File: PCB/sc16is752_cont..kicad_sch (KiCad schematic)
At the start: 66 parts, among them IC13 SN74LVC1G125DBVT, IC14 LM3940IMP-3.3_NOPB, IC15 SN74LVC1G125DBVT, IC8 LMR33640ADDAR, J3 5747842-2, J4 Screw_Terminal_01x02, J5 Screw_Terminal_01x02, J6 5747842-2, Q1 SQ2319ADS-T1_BE3, Y2 ASE-14.7456MHZ-LC-T

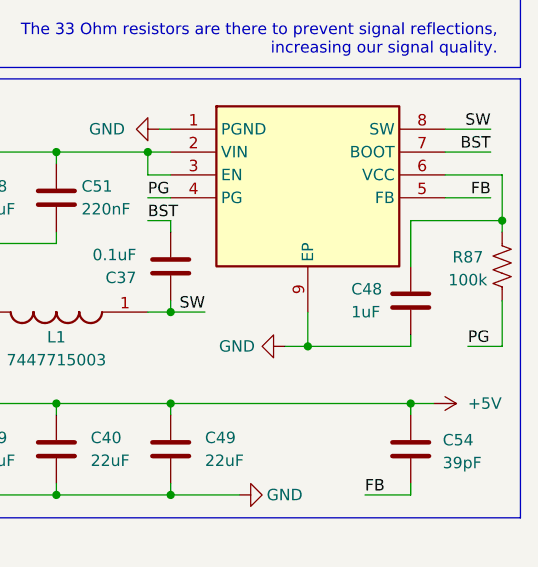
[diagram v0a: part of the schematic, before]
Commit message: Board Modifications and Initial Comms w/ Sensors
Modified wiring to separate ethernet reset from SC16 reset, adjusted pinouts and power, worked on code to get board talking to sensors. Ethernet still needs a bodge wire at this point.
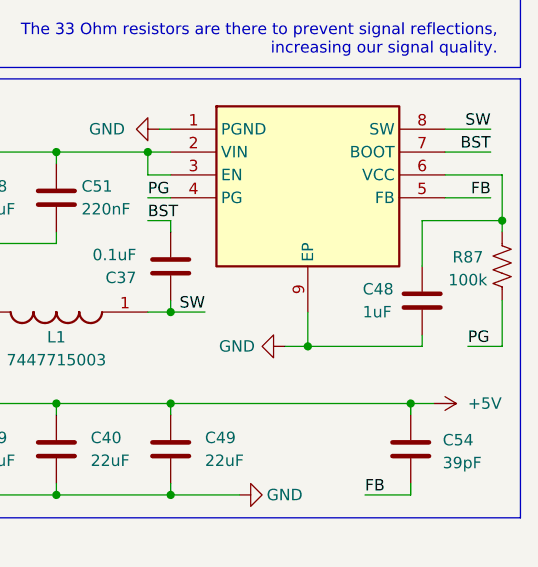
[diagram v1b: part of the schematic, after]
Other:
- moved on the sheet: C48
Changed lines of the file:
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@@
 	(wire
 		(pts
-			(xy 271.78 132.08) (xy 271.78 137.16)
+			(xy 273.05 132.08) (xy 273.05 137.16)
 		)
 		(stroke
@@
 	(wire
 		(pts
-			(xy 271.78 144.78) (xy 271.78 146.05)
+			(xy 273.05 144.78) (xy 273.05 146.05)
 		)
 		(stroke
@@
 	(wire
 		(pts
-			(xy 271.78 132.08) (xy 281.94 132.08)
+			(xy 273.05 132.08) (xy 281.94 132.08)
 		)
 		(stroke
@@
 	(wire
 		(pts
-			(xy 260.35 146.05) (xy 271.78 146.05)
+			(xy 260.35 146.05) (xy 273.05 146.05)
 		)
 		(stroke
@@
 	(symbol
 		(lib_id "Device:C")
-		(at 271.78 140.97 180)
+		(at 273.05 140.97 180)
 		(unit 1)
 		(body_style 1)
@@
 		(dnp no)
 		(property "Reference" "C48"
-			(at 265.176 139.7 0)
+			(at 266.446 139.7 0)
 			(show_name no)
 			(do_not_autoplace no)
@@
 		)
 		(property "Value" "1uF"
-			(at 265.176 142.24 0)
+			(at 266.446 142.24 0)
 			(show_name no)
 			(do_not_autoplace no)
@@
 		)
 		(property "Footprint" "Capacitor_SMD:C_0805_2012Metric_Pad1.18x1.45mm_HandSolder"
-			(at 270.8148 137.16 0)
+			(at 272.0848 137.16 0)
 			(hide yes)
 			(show_name no)
@@
 		)
 		(property "Datasheet" ""
-			(at 271.78 140.97 0)
+			(at 273.05 140.97 0)
 			(hide yes)
 			(show_name no)
@@
 		)
 		(property "Description" "Unpolarized capacitor"
-			(at 271.78 140.97 0)
+			(at 273.05 140.97 0)
 			(hide yes)
 			(show_name no)
@@
 		)
 		(property "Manufacturer_Part_Number" "CL21B105KOFNNWE"
-			(at 271.78 140.97 0)
+			(at 273.05 140.97 0)
 			(hide yes)
 			(show_name no)
@@
 		)
 		(property "Mouser Part Number" "187-CL21B105KOFNNWE"
-			(at 271.78 140.97 0)
+			(at 273.05 140.97 0)
 			(hide yes)
 			(show_name no)
@@
 		)
 		(property "Maunfacturer Part Number" ""
-			(at 271.78 140.97 0)
+			(at 273.05 140.97 0)
 			(hide yes)
 			(show_name no)
@@
 		)
 		(property "AVAILABILITY" ""
-			(at 271.78 140.97 0)
+			(at 273.05 140.97 0)
 			(hide yes)
 			(show_name no)
@@
 		)
 		(property "Check_prices" ""
-			(at 271.78 140.97 0)
+			(at 273.05 140.97 0)
 			(hide yes)
 			(show_name no)
@@
 		)
 		(property "MF" ""
-			(at 271.78 140.97 0)
+			(at 273.05 140.97 0)
 			(hide yes)
 			(show_name no)
@@
 		)
 		(property "MP" ""
-			(at 271.78 140.97 0)
+			(at 273.05 140.97 0)
 			(hide yes)
 			(show_name no)
@@
 		)
 		(property "Maunfacturer_Part_Number" ""
-			(at 271.78 140.97 0)
+			(at 273.05 140.97 0)
 			(hide yes)
 			(show_name no)
@@
 		)
 		(property "PACKAGE" ""
-			(at 271.78 140.97 0)
+			(at 273.05 140.97 0)
 			(hide yes)
 			(show_name no)
@@
 		)
 		(property "PARTREV" ""
-			(at 271.78 140.97 0)
+			(at 273.05 140.97 0)
 			(hide yes)
 			(show_name no)
@@
 		)
 		(property "PRICE" ""
-			(at 271.78 140.97 0)
+			(at 273.05 140.97 0)
 			(hide yes)
 			(show_name no)
@@
 		)
 		(property "STANDARD" ""
-			(at 271.78 140.97 0)
+			(at 273.05 140.97 0)
 			(hide yes)
 			(show_name no)
@@
 		)
 		(property "SnapEDA_Link" ""
-			(at 271.78 140.97 0)
+			(at 273.05 140.97 0)
 			(hide yes)
 			(show_name no)

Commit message: Updated PDF schematic, tweaked connections
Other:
- note added: "This oscillator module is used for timing the SC16IS752. Clock Speed: 14.7456 MHz"
- note removed: "This oscillator module is used for timing of the SC16IS752. Clock Speed: 14.7456 MHz"
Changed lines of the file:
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@@
 		)
 	)
-	(text "This oscillator module is used for timing of the SC16IS752.\n\nClock Speed: 14.7456 MHz\n"
+	(text "This oscillator module is used for timing the SC16IS752.\n\nClock Speed: 14.7456 MHz\n"
 		(exclude_from_sim no)
 		(at 72.644 66.802 0)

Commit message: Touch-ups
Various minor improvements
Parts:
- added F3: 1206L075SLYR, Fuse:Fuse_1206_3216Metric, symbol 1206L075SLYR:1206L075SLYR
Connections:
- net +3V3: now also F3.2; no longer C33.1, C35.2, IC14.3 (OUT)
- new net 3V3OUT: C33.1, C35.2, F3.1, IC14.3 (OUT)
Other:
- moved on the sheet: C32, C33, C35, IC14
